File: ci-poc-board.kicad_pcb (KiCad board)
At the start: 4 copper layers, 88.9 x 40.6 mm, 39 parts, among them J1 Conn_Coaxial, J2 Conn_01x05_USART_1, J3 Conn_01x05_USART_2, J4 Conn_01x05_USART_3, J5 Conn_01x05_I2C_0, J7 Conn_01x02_BATT, J8 Conn_02x05_Counter_Clockwise_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, SW1 SW_Push, U1 ATSAMD21G18A-A, U2 LD1117S33TR_SOT223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

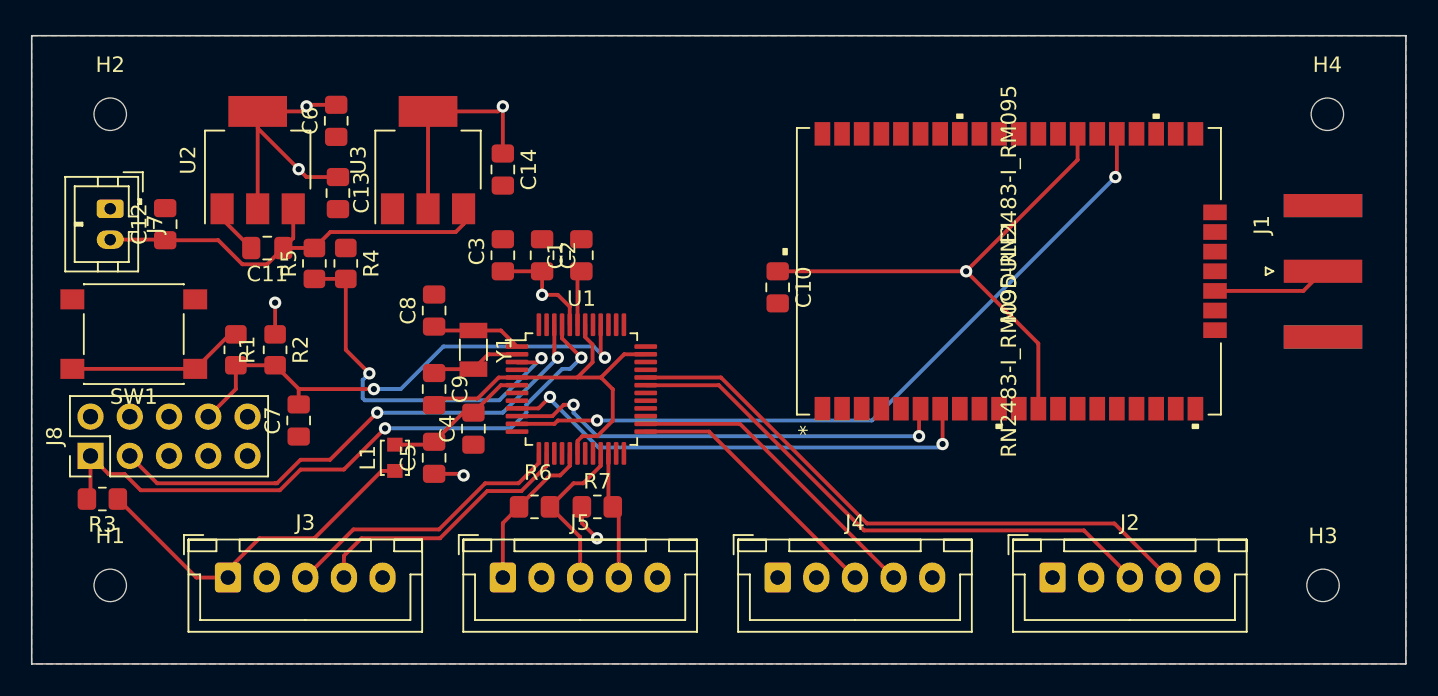
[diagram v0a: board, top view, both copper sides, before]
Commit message: Moved SMA connector to the edge
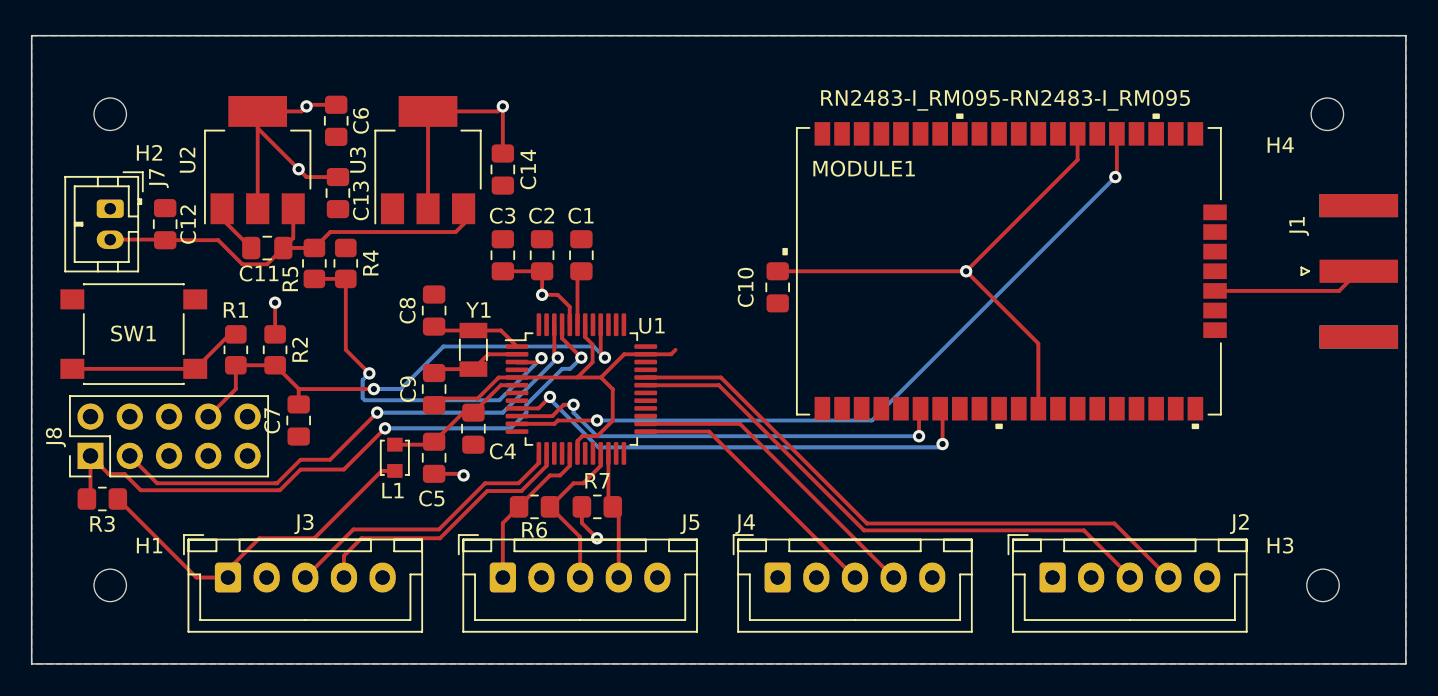
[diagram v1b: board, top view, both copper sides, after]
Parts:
- moved J1 2.31 mm to (144.3, 63.5)
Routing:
- net Net-(J1-Pad1): track 7.51 -> 9.83 mm
- net GND: track 31.1 -> 33.1 mm

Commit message: Small changes. Added BOM
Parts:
- H1, H2, H3, H4: footprint MountingHole:MountingHole_2.1mm -> MountingHole:MountingHole_3.2mm_M3_DIN965_Pad
- MODULE1: footprint RN2483:RN2483A-I&slash_RM105 -> RF_Module:RN2483
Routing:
- net VDDIN: track 98.2 -> 74.4 mm, vias 6 -> 11
- net +5V: track 14.9 -> 21.3 mm, vias 1 -> 4
- net RN2483_RESET: track 48.2 -> 51.0 mm

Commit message: Added title and date to PCB, added render to README.md
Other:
- board text added: "Connected Islands PoC Board"
- board text added: "V1.0 10-03-2022 Made by Daan Dekoning"
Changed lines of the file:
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@@
       (layerselection 0x00010fc_ffffffff)
       (disableapertmacros false)
-      (usegerberextensions false)
+      (usegerberextensions true)
       (usegerberattributes true)
-      (usegerberadvancedattributes true)
+      (usegerberadvancedattributes false)
       (creategerberjobfile true)
       (svguseinch false)
@@
       (psa4output false)
       (plotreference true)
-      (plotvalue true)
+      (plotvalue false)
       (plotinvisibletext false)
       (sketchpadsonfab false)
-      (subtractmaskfromsilk false)
-      (outputformat 4)
+      (subtractmaskfromsilk true)
+      (outputformat 1)
       (mirror false)
       (drillshape 0)
       (scaleselection 1)
-      (outputdirectory "")
+      (outputdirectory "ci-poc-board-gerbers")
     )
   )
@@
     (property "Sheetname" "")
     (attr smd)
-    (fp_text reference "R3" (at 0 -1.65) (layer "F.SilkS")
+    (fp_text reference "R3" (at -2.921 -0.381) (layer "F.SilkS")
       (effects (font (size 1 1) (thickness 0.15)))
     )
@@
   )
   (gr_rect (start 58.42 48.26) (end 147.32 88.9) (layer "Edge.Cuts") (width 0.1) (fill none))
+  (gr_text "Connected Islands PoC Board" (at 115.189 50.8) (layer "F.SilkS")
+    (effects (font (size 2 2) (thickness 0.15)))
+  )
+  (gr_text "V1.0 10-03-2022\nMade by Daan Dekoning" (at 92.837 53.34) (layer "F.SilkS")
+    (effects (font (size 0.75 0.75) (thickness 0.15)) (justify left))
+  )
   (segment (start 93.73 63.75) (end 93.73 66.9575) (width 0.25) (layer "F.Cu") (net 1))
   (segment (start 93.98 63.5) (end 93.73 63.75) (width 0.25) (layer "F.Cu") (net 1))

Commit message: Make KiCad project more portable
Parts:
- C1, C10, C11, C12, C13, C14, C2, C3, C4, C5, C6, C7, C8, C9: footprint Capacitor_SMD:C_0805_2012Metric_Pad1.18x1.45mm_HandSolder -> lib_fp:C_0805_2012Metric_Pad1.18x1.45mm_HandSolder
- H1, H2, H3, H4: footprint MountingHole:MountingHole_3.2mm_M3_DIN965_Pad -> lib_fp:MountingHole_3.2mm_M3_DIN965_Pad
- J1: footprint Connector_Coaxial:SMA_Amphenol_132289_EdgeMount -> lib_fp:SMA_Amphenol_132289_EdgeMount
- J2, J3, J4, J5: footprint Connector_JST:JST_XH_B5B-XH-A_1x05_P2.50mm_Vertical -> lib_fp:JST_XH_B5B-XH-A_1x05_P2.50mm_Vertical
- J7: footprint Connector_JST:JST_PH_B2B-PH-K_1x02_P2.00mm_Vertical -> lib_fp:JST_PH_B2B-PH-K_1x02_P2.00mm_Vertical
- J8: footprint Connector_PinHeader_2.54mm:PinHeader_2x05_P2.54mm_Vertical -> lib_fp:PinHeader_2x05_P2.54mm_Vertical
- L1: footprint Inductor_SMD:L_Murata_LQH2MCNxxxx02_2.0x1.6mm -> lib_fp:L_Murata_LQH2MCNxxxx02_2.0x1.6mm
- MODULE1: footprint RF_Module:RN2483 -> lib_fp:RN2483
- R1, R2, R3, R4, R5, R6, R7: footprint Resistor_SMD:R_0805_2012Metric_Pad1.20x1.40mm_HandSolder -> lib_fp:R_0805_2012Metric_Pad1.20x1.40mm_HandSolder
- SW1: footprint Button_Switch_SMD:SW_Push_1P1T_NO_6x6mm_H9.5mm -> lib_fp:SW_Push_1P1T_NO_6x6mm_H9.5mm
- U1: footprint Package_QFP:TQFP-48_7x7mm_P0.5mm -> lib_fp:TQFP-48_7x7mm_P0.5mm
- U2, U3: footprint Package_TO_SOT_SMD:SOT-223-3_TabPin2 -> lib_fp:SOT-223-3_TabPin2
- Y1: footprint Crystal:Crystal_SMD_3215-2Pin_3.2x1.5mm -> lib_fp:Crystal_SMD_3215-2Pin_3.2x1.5mm
